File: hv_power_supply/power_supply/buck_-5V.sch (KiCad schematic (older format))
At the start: 4 parts

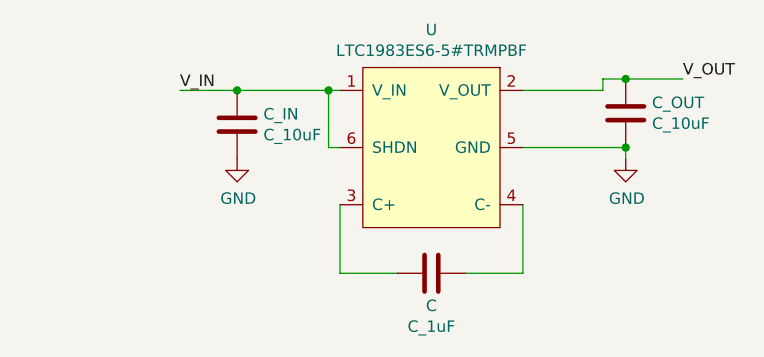
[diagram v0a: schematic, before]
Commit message: updated MCU pins
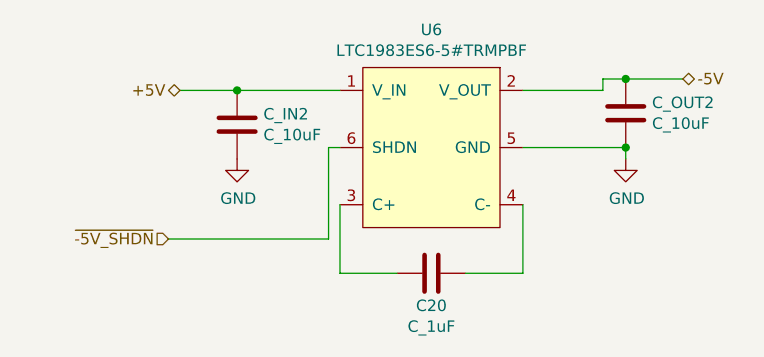
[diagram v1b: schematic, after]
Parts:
- renumbered C to C20, C_IN to C_IN2, C_OUT to C_OUT2, U to U6
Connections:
- net V_IN renamed +5V
- net +5V: no longer U6.6 (SHDN)
- net V_OUT renamed -5V
- new net ~-5V_SHDN: U6.6 (SHDN)
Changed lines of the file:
@@
 $Descr A4 11693 8268
 encoding utf-8
-Sheet 1 1
+Sheet 5 6
 Title ""
 Date ""
@@
 $EndDescr
 $Comp
-L formula:LTC1983ES6-5#TRMPBF U
+L formula:LTC1983ES6-5#TRMPBF U6
 U 1 1 6057CB8B
 P 5200 3000
-F 0 "U" H 5200 3465 50  0000 C CNN
+F 0 "U6" H 5200 3465 50  0000 C CNN
 F 1 "LTC1983ES6-5#TRMPBF" H 5200 3374 50  0000 C CNN
 F 2 "" H 5200 3400 50  0001 C CNN
@@
 	1    0    0    -1
 $EndComp
-Wire Wire Line
-	4350 2800 4750 2800
 $Comp
-L formula:C_10uF C_IN
+L formula:C_10uF C_IN2
 U 1 1 60587A61
 P 4350 3000
-F 0 "C_IN" H 4465 3096 50  0000 L CNN
+F 0 "C_IN2" H 4465 3096 50  0000 L CNN
 F 1 "C_10uF" H 4465 3005 50  0000 L CNN
 F 2 "footprints:C_0805_OEM" H 4388 3600 50  0001 C CNN
@@
 $EndComp
 $Comp
-L formula:C_10uF C_OUT
+L formula:C_10uF C_OUT2
 U 1 1 6058529E
 P 6050 2950
-F 0 "C_OUT" H 6165 3046 50  0000 L CNN
+F 0 "C_OUT2" H 6165 3046 50  0000 L CNN
 F 1 "C_10uF" H 6165 2955 50  0000 L CNN
 F 2 "footprints:C_0805_OEM" H 6088 3550 50  0001 C CNN
@@
 	1    0    0    -1
 $EndComp
-Text Label 6300 2750 0    50   ~ 0
-V_OUT
 Wire Wire Line
 	4100 2800 4350 2800
-Text Label 4100 2800 0    50   ~ 0
-V_IN
 Connection ~ 4350 2800
 $Comp
-L power:GND #PWR?
+L power:GND #PWR049
 U 1 1 605913B8
 P 6050 3100
-F 0 "#PWR?" H 6050 2850 50  0001 C CNN
+F 0 "#PWR049" H 6050 2850 50  0001 C CNN
 F 1 "GND" H 6055 2927 50  0000 C CNN
 F 2 "" H 6050 3100 50  0001 C CNN
@@
 $EndComp
 $Comp
-L power:GND #PWR?
+L power:GND #PWR048
 U 1 1 60591FE0
 P 4350 3100
-F 0 "#PWR?" H 4350 2850 50  0001 C CNN
+F 0 "#PWR048" H 4350 2850 50  0001 C CNN
 F 1 "GND" H 4355 2927 50  0000 C CNN
 F 2 "" H 4350 3100 50  0001 C CNN
@@
 $EndComp
 $Comp
-L formula:C_1uF C
+L formula:C_1uF C20
 U 1 1 6059D072
 P 5250 3600
-F 0 "C" V 5108 3650 50  0000 C CNN
+F 0 "C20" V 5108 3650 50  0000 C CNN
 F 1 "C_1uF" V 5017 3650 50  0000 C CNN
 F 2 "footprints:C_0805_OEM" H 5288 4200 50  0001 C CNN
@@
 	4800 3050 4750 3050
 Wire Wire Line
-	4750 3050 4750 2800
-Connection ~ 4750 2800
-Wire Wire Line
-	4750 2800 4800 2800
-Wire Wire Line
 	6050 3050 6050 3100
 Connection ~ 6050 3050
+Text HLabel 4100 2800 0    50   BiDi ~ 0
++5V
+Text HLabel 6300 2750 2    50   BiDi ~ 0
+-5V
+Wire Wire Line
+	4350 2800 4800 2800
+Wire Wire Line
+	4750 3050 4750 3450
+Wire Wire Line
+	4750 3450 4050 3450
+Text HLabel 4050 3450 0    50   Input ~ 0
+~-5V_SHDN
 $EndSCHEMATC

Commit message: Fixed all component footprint issues, beginning to lay out flyback portion
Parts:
- U6: footprint (none) -> footprints:LTC1983ES6-5#TRMPBF; Manufacturer (none) -> Analog Devices Inc.; Manufacturer Product Number (none) -> LTC1983ES6-5#TRMPBF; Purchasing Link (none) -> https://www.digikey.com/en/products/detail/analog-devices-i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
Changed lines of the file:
@@
 $EndDescr
-$Comp
-L formula:LTC1983ES6-5#TRMPBF U6
-U 1 1 6057CB8B
-P 5200 3000
-F 0 "U6" H 5200 3465 50  0000 C CNN
-F 1 "LTC1983ES6-5#TRMPBF" H 5200 3374 50  0000 C CNN
-F 2 "" H 5200 3400 50  0001 C CNN
-F 3 "" H 5200 3400 50  0001 C CNN
-	1    5200 3000
-	1    0    0    -1
-$EndComp
 $Comp
 L formula:C_10uF C_IN2
@@
 Text HLabel 4050 3450 0    50   Input ~ 0
 ~-5V_SHDN
+$Comp
+L formula:LTC1983ES6-5#TRMPBF U6
+U 1 1 6063998C
+P 5200 3000
+F 0 "U6" H 5200 3465 50  0000 C CNN
+F 1 "LTC1983ES6-5#TRMPBF" H 5200 3374 50  0000 C CNN
+F 2 "footprints:LTC1983ES6-5#TRMPBF" H 5200 3400 50  0001 C CNN
+F 3 "https://www.analog.com/media/en/technical-documentation/data-sheets/1983fc.pdf" H 5200 3400 50  0001 C CNN
+F 4 "https://www.digikey.com/en/products/detail/analog-devices-inc/LTC1983ES6-5-TRMPBF/1115931" H 5200 3000 50  0001 C CNN "Purchasing Link"
+F 5 "Analog Devices Inc." H 5200 3000 50  0001 C CNN "Manufacturer"
+F 6 "LTC1983ES6-5#TRMPBF" H 5200 3000 50  0001 C CNN "Manufacturer Product Number"
+	1    5200 3000
+	1    0    0    -1
+$EndComp
 $EndSCHEMATC
